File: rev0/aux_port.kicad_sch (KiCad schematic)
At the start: 22 parts, among them IC1 ECP5-BGA256, U11 USB3343-CP, U12 FUSB302BMPX

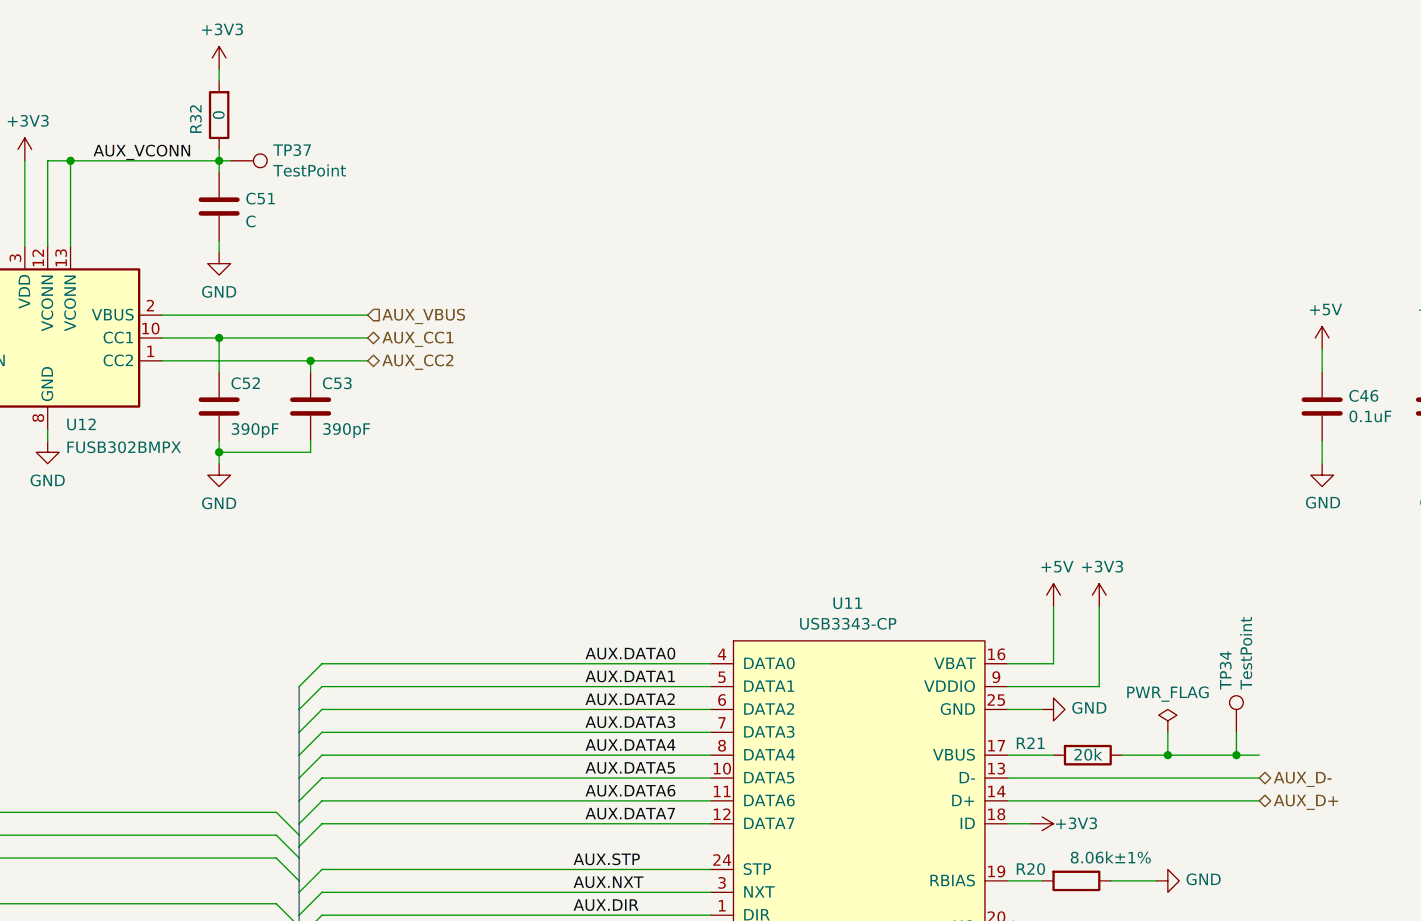
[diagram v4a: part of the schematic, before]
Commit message: hardware: clamp VBUS detection signals to 24 V
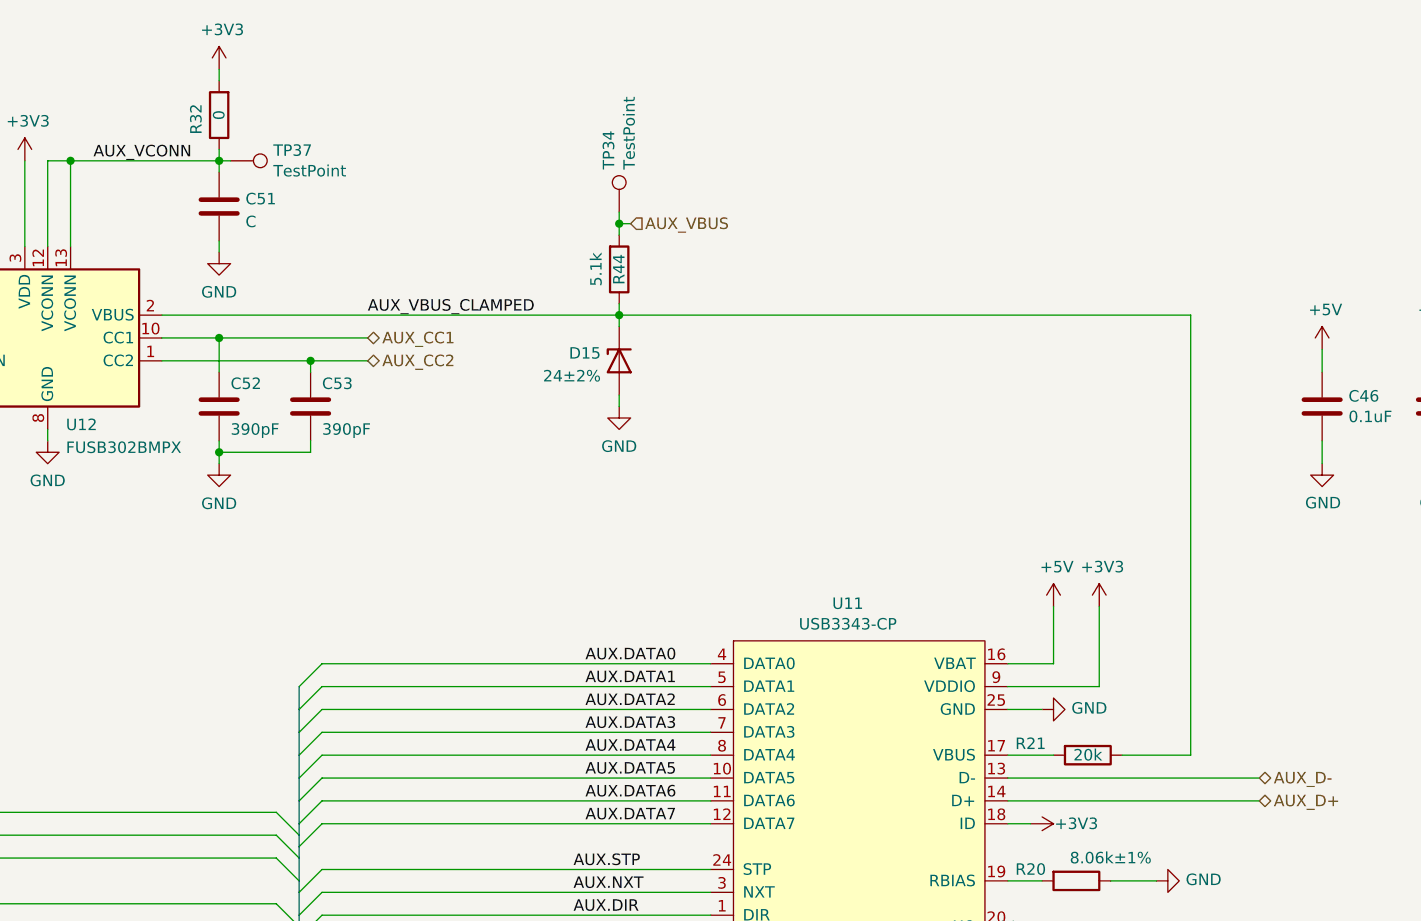
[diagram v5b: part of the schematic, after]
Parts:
- added D15: 24±2%, luna:DFN1006-2, symbol Device:D_Zener
- added R44: 5.1k, Resistor_SMD:R_0402_1005Metric, symbol Device:R
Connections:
- net AUX_VBUS: now also TP34.1, R44.2; no longer U12.2 (VBUS)
- net GND: now also D15.2 (A)
- net AUX_VBUS_CLAMPED: now reaches R21.1
- net AUX_VBUS_CLAMPED: now also U12.2 (VBUS), D15.1 (K), R44.1; no longer TP34.1
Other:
- moved on the sheet: TP34

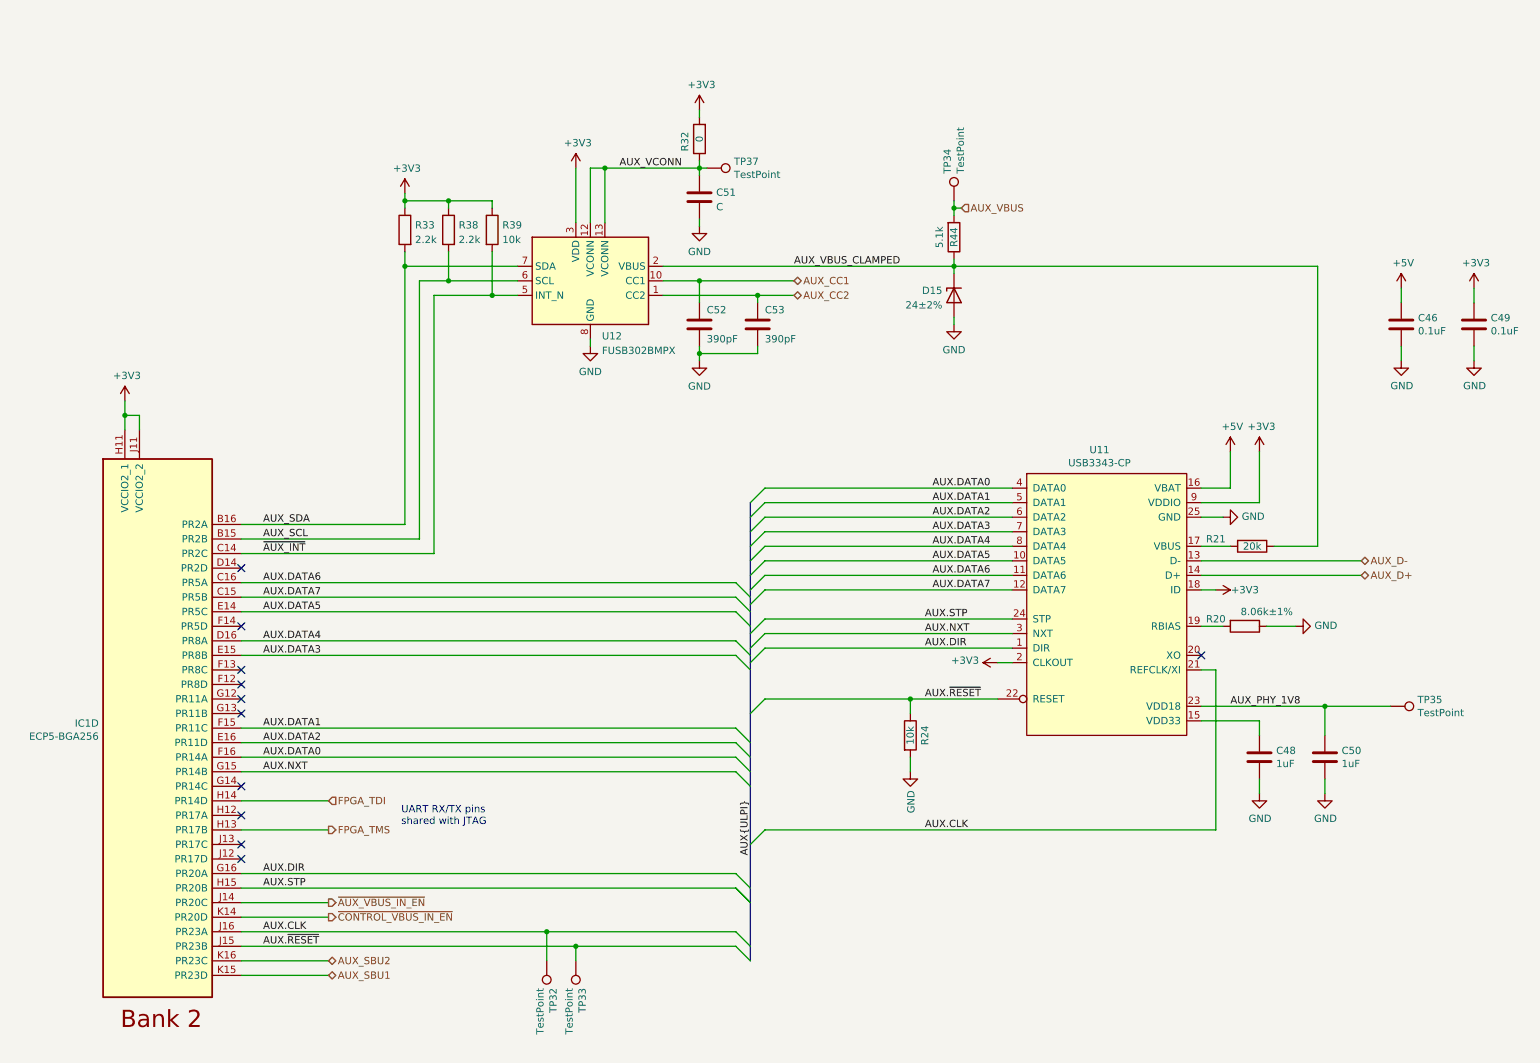
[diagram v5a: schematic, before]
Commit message: hardware: protect CC and SBU pins
add overvoltage and ESD protection for Aux port and Target port USB
Type-C CC and SBU pins
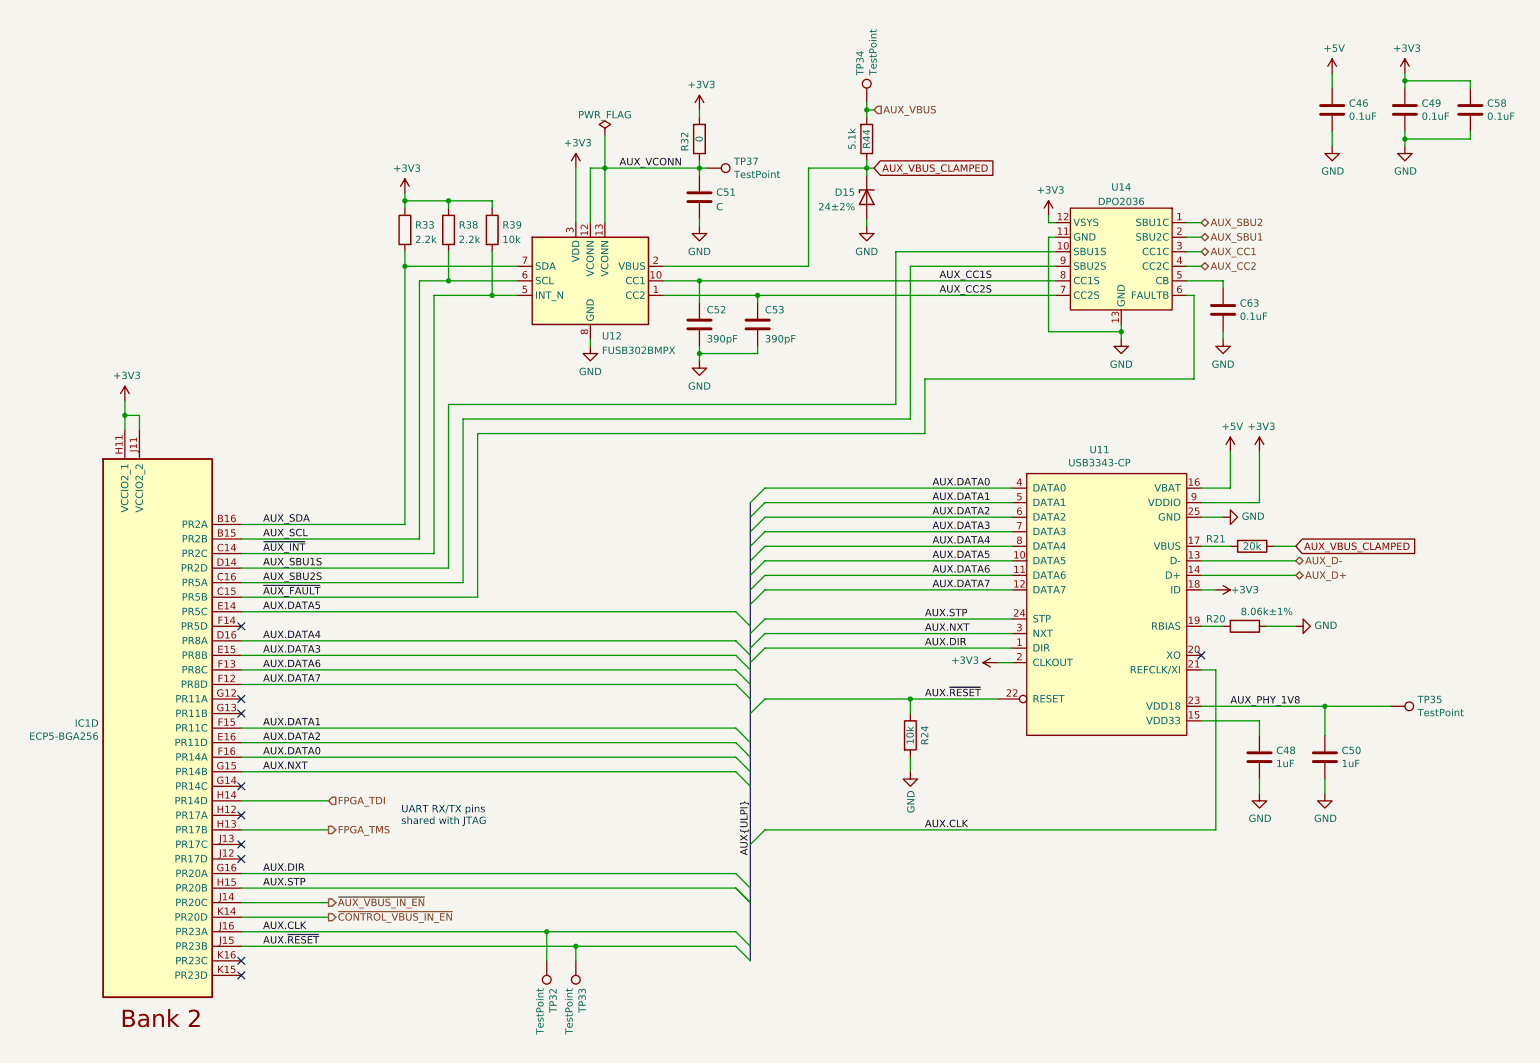
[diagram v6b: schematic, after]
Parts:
- added C58, C63: 0.1uF, Capacitor_SMD:C_0402_1005Metric, symbol Device:C
- added U14: DPO2036, luna:Diodes_UQFN2020-12_Type-B, symbol usb:DPO2036
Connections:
- net +3V3: now also C58.1, U14.12 (VSYS)
- net AUX.DATA6: now also IC1.F13 (PR8C); no longer IC1.C16 (PR5A)
- net AUX.DATA7: now also IC1.F12 (PR8D); no longer IC1.C15 (PR5B)
- net AUX_CC1: now also U14.3 (CC1C); no longer C52.1, U12.10 (CC1), U12.11 (CC1)
- net AUX_CC2: now also U14.4 (CC2C); no longer C53.1, U12.1 (CC2), U12.14 (CC2)
- net AUX_SBU1: now also U14.2 (SBU2C); no longer IC1.K15 (PR23D)
- net AUX_SBU2: now also U14.1 (SBU1C); no longer IC1.K16 (PR23C)
- net GND: now also C58.2, C63.2, U14.11 (GND), U14.13 (GND)
- net AUX_SBU1S: now reaches IC1.D14 (PR2D)
- net AUX_SBU1S: now also U14.10 (SBU1S)
- new net: C63.1, U14.5 (CB)
- new net AUX_CC1S: C52.1, U12.10 (CC1), U12.11 (CC1), U14.8 (CC1S)
- new net AUX_CC2S: C53.1, U12.1 (CC2), U12.14 (CC2), U14.7 (CC2S)
- new net AUX_SBU2S: IC1.C16 (PR5A), U14.9 (SBU2S)
- new net ~{AUX_FAULT}: IC1.C15 (PR5B), U14.6 (FAULTB)
- no-connect marks 11 -> 10
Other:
- moved on the sheet: C46, C49, D15, R44, TP34

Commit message: hardware: use "Exclude from bill of materials"
Virtual components such as mounting holes and test points that do not
require part placement now use this property instead of the DNP field.
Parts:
- TP32, TP33, TP34, TP35, TP37: DNP DNP -> (none); now left out of the parts list
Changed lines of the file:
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@@
   )
   (symbol (lib_id "Connector:TestPoint") (at 260.35 132.08 270) (unit 1)
-    (in_bom yes) (on_board yes)
+    (in_bom no) (on_board yes)
     (property "Reference" "TP35" (id 0) (at 265.0998 130.937 90)
       (effects (font (size 1.27 1.27)) (justify left))
@@
       (effects (font (size 1.27 1.27)) hide)
     )
-    (property "DNP" "DNP" (id 4) (at 260.35 132.08 0)
-      (effects (font (size 1.27 1.27)) hide)
-    )
     (pin "1")
   )
   (symbol (lib_id "Connector:TestPoint") (at 168.91 26.67 0) (unit 1)
-    (in_bom yes) (on_board yes)
+    (in_bom no) (on_board yes)
     (property "Reference" "TP34" (id 0) (at 167.767 21.9202 90)
       (effects (font (size 1.27 1.27)) (justify left))
@@
       (effects (font (size 1.27 1.27)) hide)
     )
-    (property "DNP" "DNP" (id 4) (at 168.91 26.67 0)
-      (effects (font (size 1.27 1.27)) hide)
-    )
     (pin "1")
   )
   (symbol (lib_id "Connector:TestPoint") (at 118.11 176.53 180) (unit 1)
-    (in_bom yes) (on_board yes)
+    (in_bom no) (on_board yes)
     (property "Reference" "TP33" (id 0) (at 119.253 181.2798 90)
       (effects (font (size 1.27 1.27)) (justify left))
@@
       (effects (font (size 1.27 1.27)) hide)
     )
-    (property "DNP" "DNP" (id 4) (at 118.11 176.53 0)
-      (effects (font (size 1.27 1.27)) hide)
-    )
     (pin "1")
   )
   (symbol (lib_id "Connector:TestPoint") (at 113.03 176.53 180) (unit 1)
-    (in_bom yes) (on_board yes)
+    (in_bom no) (on_board yes)
     (property "Reference" "TP32" (id 0) (at 114.173 181.2798 90)
       (effects (font (size 1.27 1.27)) (justify left))
@@
     )
     (property "Datasheet" "~" (id 3) (at 107.95 176.53 0)
-      (effects (font (size 1.27 1.27)) hide)
-    )
-    (property "DNP" "DNP" (id 4) (at 113.03 176.53 0)
       (effects (font (size 1.27 1.27)) hide)
     )
@@
   )
   (symbol (lib_id "Connector:TestPoint") (at 140.97 38.1 270) (unit 1)
-    (in_bom yes) (on_board yes)
+    (in_bom no) (on_board yes)
     (property "Reference" "TP37" (id 0) (at 145.7198 36.957 90)
       (effects (font (size 1.27 1.27)) (justify left))
@@
       (effects (font (size 1.27 1.27)) hide)
     )
-    (property "DNP" "DNP" (id 4) (at 140.97 38.1 0)
-      (effects (font (size 1.27 1.27)) hide)
-    )
